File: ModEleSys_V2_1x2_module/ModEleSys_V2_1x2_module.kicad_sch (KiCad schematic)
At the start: 4 parts, among them J1 module_2x15_left_input, J2 module_2x15_right_input

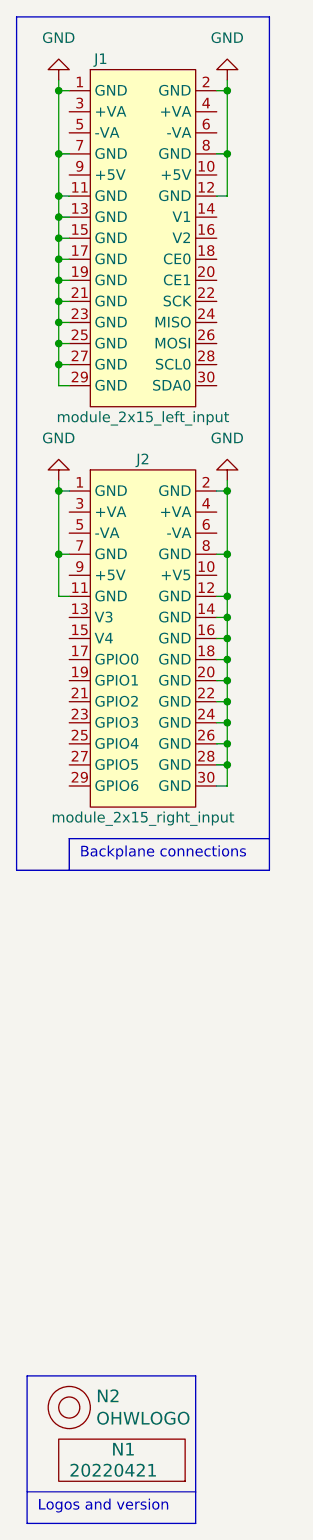
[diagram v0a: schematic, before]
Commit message: completed ModEleSys V2 1x2 sized module
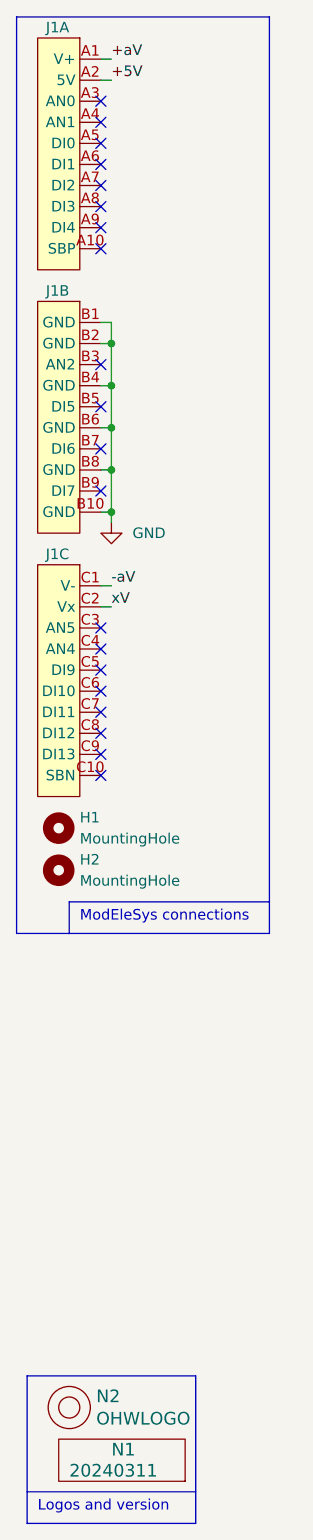
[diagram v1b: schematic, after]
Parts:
- removed J1: module_2x15_left_input, SquantorConnectorsNamed:module_2x15_left, symbol SquantorConnectorsNamed:module_2x15_left_input
- removed J2: module_2x15_right_input, SquantorConnectorsNamed:module_2x15_right, symbol SquantorConnectorsNamed:module_2x15_right_input
- added H1, H2: MountingHole, SquantorPcbOutline:MountingHole_3.2mm_M3_Pad_Via, symbol Mechanical:MountingHole
- added J1: ~, SquantorConnectors:DIN41612_R3_3x10_Male_Vertical_THT, symbol SquantorConnectorsNamed:SquMes_30pin
- N1: value 20220421 -> 20240311
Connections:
- net GND: now also J1.B1 (GND), J1.B10 (GND), J1.B2 (GND), J1.B4 (GND), J1.B6 (GND), J1.B8 (GND)
- new net +5V: J1.A2 (5V)
- new net +aV: J1.A1 (V+)
- new net -aV: J1.C1 (V-)
- new net xV: J1.C2 (Vx)
- no-connect marks 0 -> 20
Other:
- note added: "ModEleSys connections"
- note removed: "Backplane connections"
